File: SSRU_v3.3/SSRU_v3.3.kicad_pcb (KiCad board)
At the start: 2 copper layers, 95 x 78 mm, 64 parts, among them J2 Conn_01x24, J4 AVR-ISP-6, SW1 SW_Push, U10 TJA1051T, U2 ATmega328P-A, U3 SGM722, U4 LM2576S-5, U6 MCP2515-xST, U69 SGM722, Y1 16MHz, Y4 20MHz

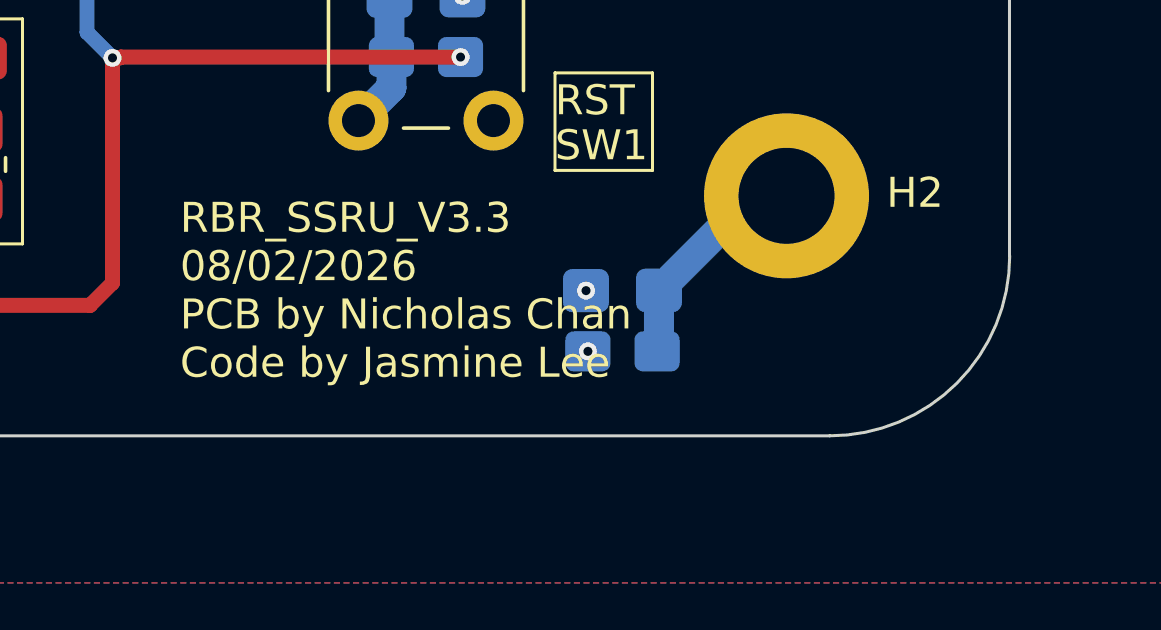
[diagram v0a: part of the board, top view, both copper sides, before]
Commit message: Update KiCad project metadata and silkscreen
Remove obsolete B.SilkS rectangle elements and update front silkscreen text to credit both Nicholas and Jasmine. Refresh project preference and metadata files for newer KiCad format: change active_layer_preset to "All Layers", replace numeric visible_items with named entries, expand visible_layers mask, and bump .kicad_prl/.kicad_pro version fields. Also add a priority field to the Default netclass. These updates align the project files with updated KiCad settings and clean up silkscreen artifacts.
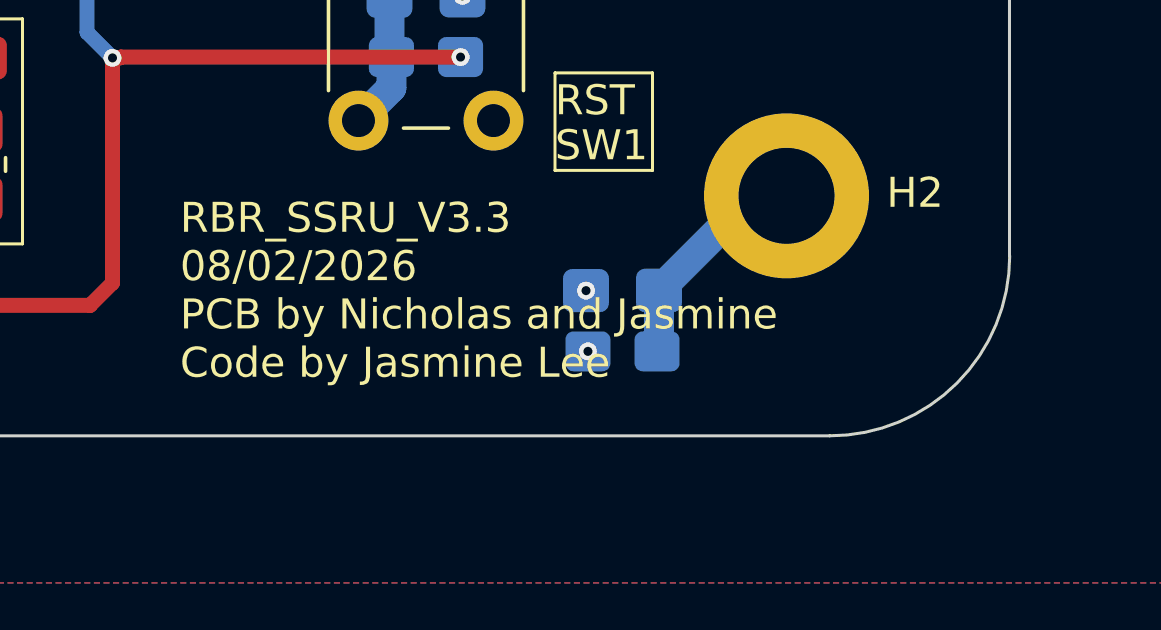
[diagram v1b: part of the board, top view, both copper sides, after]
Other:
- board text added: "RBR_SSRU_V3.3 08/02/2026 PCB by Nicholas and Jasmine Code by Jasmine Lee"
- board text removed: "RBR_SSRU_V3.3 08/02/2026 PCB by Nicholas Chan Code by Jasmine Lee"
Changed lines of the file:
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@@
-		(layer "B.SilkS")
-	)
-	(gr_rect
-		(start 121.5 109.75)
-		(end 123.5 114.25)
-		(stroke
-			(width 0.1)
-			(type default)
-		)
-		(fill no)
 		(layer "B.SilkS")
 	)
@@
 			(type default)
 		)
-		(layer "B.SilkS")
-	)
-	(gr_rect
-		(start 123.5 109.75)
-		(end 126.5 111.5)
-		(stroke
-			(width 0.1)
-			(type default)
-		)
-		(fill no)
 		(layer "B.SilkS")
 	)
@@
 		(layer "Edge.Cuts")
 	)
-	(gr_text "RBR_SSRU_V3.3\n08/02/2026\nPCB by Nicholas Chan\nCode by Jasmine Lee"
+	(gr_text "RBR_SSRU_V3.3\n08/02/2026\nPCB by Nicholas and Jasmine\nCode by Jasmine Lee"
 		(at 169.75 138.25 0)
 		(layer "F.SilkS")

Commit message: ssru gerbers
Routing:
- net +5V: track 346.0 -> 345.3 mm, vias 10 -> 9
- net DS18B20: track 82.4 -> 81.8 mm
- net GND: vias 118 -> 117
